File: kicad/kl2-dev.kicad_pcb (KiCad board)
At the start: 2 copper layers, 35.6 x 15.2 mm, 13 parts, among them P1 CONN_13, P2 CONN_13, U1 MKL26Z32VFM4, X1 CRYSTAL

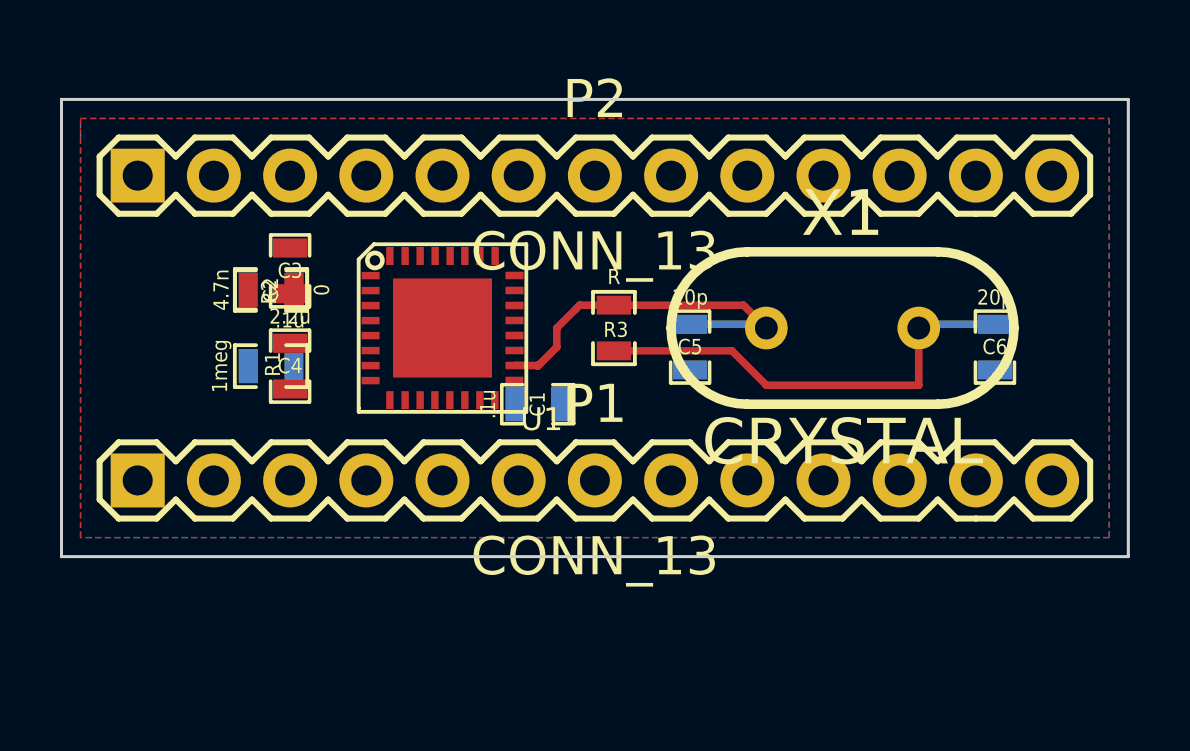
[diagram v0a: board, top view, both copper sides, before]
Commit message: Created initial board with demonstration thermal pad
We need pin 33 to be on its own special net because it shouldn't be
connected. We also have not yet routed the flows.
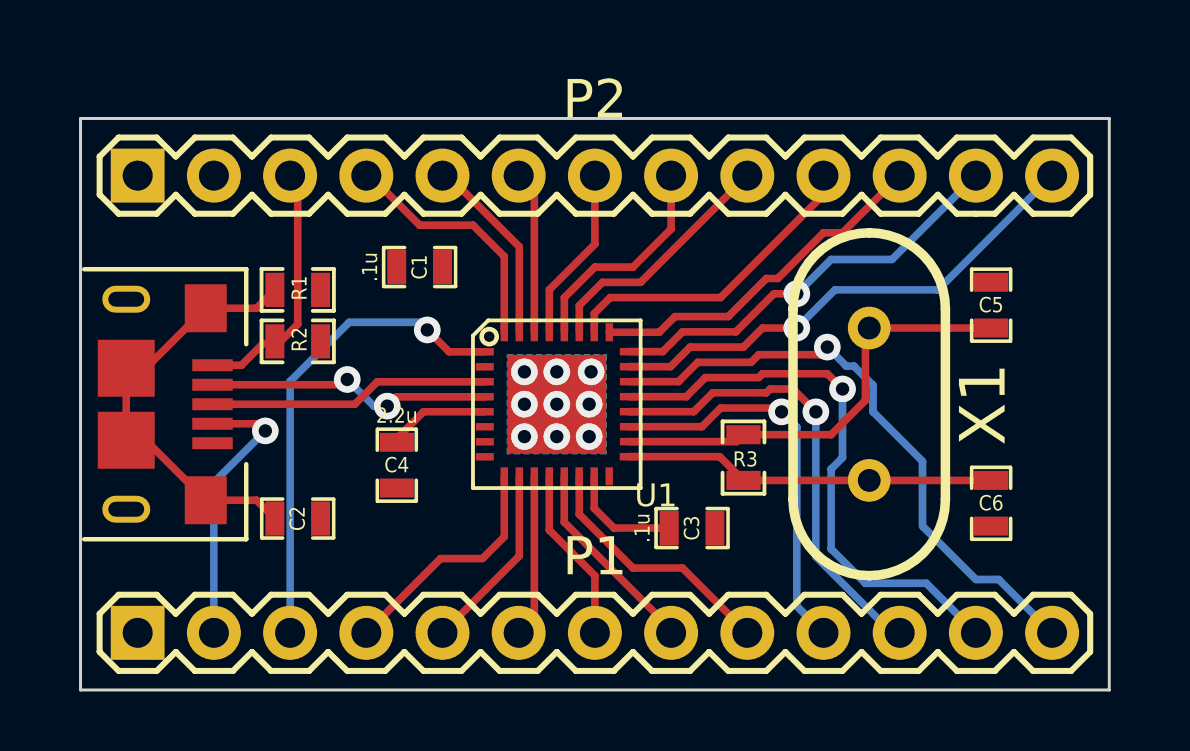
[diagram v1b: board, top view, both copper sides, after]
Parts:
- added CON1: USB-MINI-B, USB-MICRO-B, F.Cu at (36.4, 58.4)
- moved C3 15.9 mm to (55.3, 62.5), turned to 0 degrees
- moved C5 10.1 mm to (65.3, 55.1), turned to 90 degrees
- moved C2 7.67 mm to (42.2, 62.2)
- moved R3 6.11 mm to (57.0, 60.2)
- moved C1 6.03 mm to (46.2, 53.8)
- moved C6 5.21 mm to (65.3, 61.7)
- moved P1 5.08 mm to (52.1, 66.0)
- moved C4 4.85 mm to (45.5, 60.5)
- moved U1 4.58 mm to (50.8, 58.4)
- moved R1 2.69 mm to (42.2, 54.6)
- moved X1 2.69 mm to (61.2, 58.4), turned to 270 degrees
- moved R2 1.93 mm to (42.2, 56.3), turned to 0 degrees
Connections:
- U1 pad 33: (no net) -> GND
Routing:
- net /PTC1: track 0.00 -> 20.3 mm, vias 0 -> 1
- net /PTB1: track 0.00 -> 19.1 mm, vias 0 -> 1
- net /PTC2: track 0.00 -> 16.7 mm, vias 0 -> 1
- net /PTE0: track 0.00 -> 16.1 mm, vias 0 -> 1
- net /PTB0: track 0.00 -> 15.5 mm, vias 0 -> 1
- net N-0000013: track 0.00 -> 14.5 mm
- net /PTC3: track 0.00 -> 14.0 mm, vias 0 -> 1
- net /PTA20: track 0.00 -> 13.3 mm, vias 0 -> 1
- net /PTC4: track 0.00 -> 11.8 mm
- net /PTC5: track 0.00 -> 10.5 mm
- net N-0000012: track 0.00 -> 9.65 mm, vias 0 -> 2
- net N-0000011: track 0.00 -> 9.39 mm
- net /ID: track 0.00 -> 9.30 mm, vias 0 -> 1
- net /PTA4: track 0.00 -> 8.51 mm
- net /PTC6: track 0.00 -> 8.28 mm
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- removed copper zone on F.Cu, net GND
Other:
- board size 35.6 x 15.2 mm -> 34.3 x 19 mm
- net class Default: clearance 0.254 -> 0.1524
- rule trace_clearance: 0.254 -> 0.1524
- rule trace_min: 0.254 -> 0.1524

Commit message: Finished routing all but gnd and thermal pad
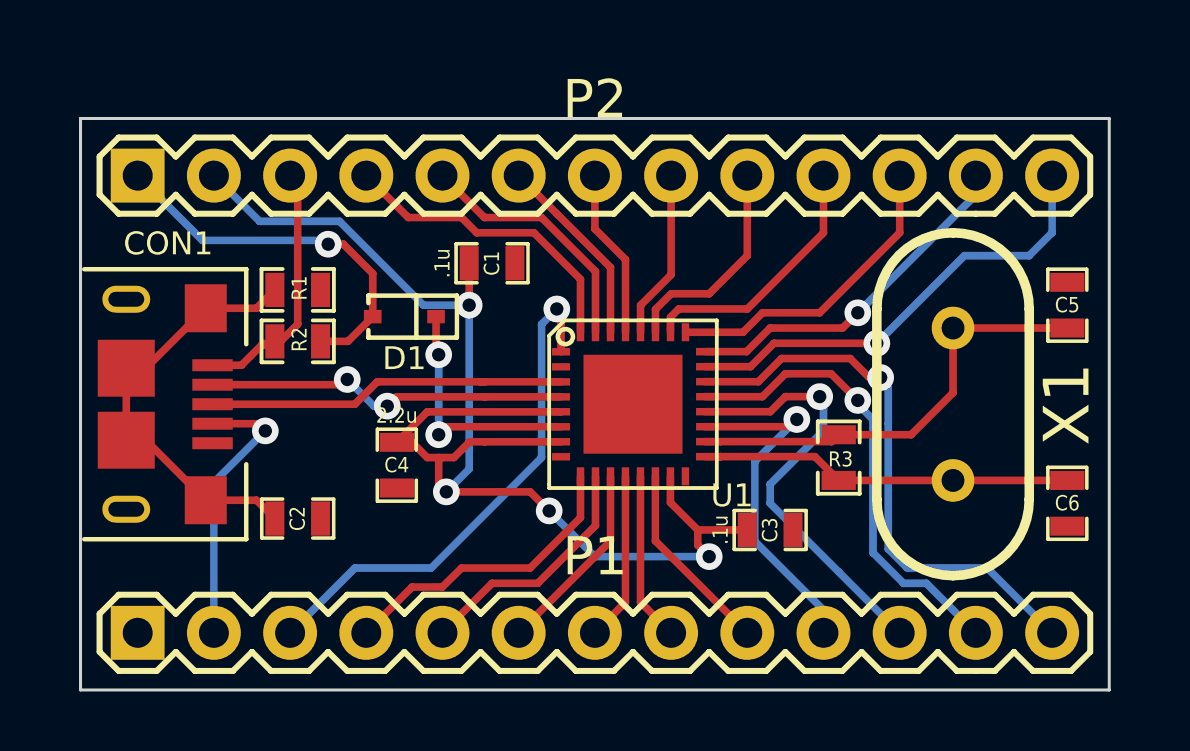
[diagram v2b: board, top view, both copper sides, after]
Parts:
- added D1: DIODE, SOD323, F.Cu at (45.7, 55.5)
- moved R3 3.17 mm to (60.2, 60.2)
- moved X1 2.79 mm to (64.0, 58.4)
- moved C3 2.60 mm to (57.9, 62.6)
- moved U1 2.54 mm to (53.3, 58.4)
- moved C5 2.54 mm to (67.8, 55.1)
- moved C6 2.54 mm to (67.8, 61.7)
- moved C1 2.42 mm to (48.6, 53.7)
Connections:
- U1 pad 33: GND -> /U1_THERM
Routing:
- net +3.3V: track 7.27 -> 45.8 mm, vias 0 -> 4
- net VDD: track 0.00 -> 12.7 mm, vias 0 -> 1
- net N-0000014: track 0.00 -> 8.16 mm, vias 0 -> 2
- net /PTB1: track 19.1 -> 15.6 mm
- net N-0000011: track 9.39 -> 12.1 mm
- net N-0000012: track 9.65 -> 12.2 mm
- net /PTC3: track 14.0 -> 11.8 mm
- net /PTE30: track 7.94 -> 10.1 mm
- net /PTD7: track 8.24 -> 10.3 mm
- net /PTD6: track 6.39 -> 8.45 mm
- net /PTA4: track 8.51 -> 6.49 mm
- net /PTA0: track 6.28 -> 8.22 mm
- net /PTC5: track 10.5 -> 8.67 mm
- net /PTC7: track 7.44 -> 5.64 mm
- net /PTA20: track 13.3 -> 11.8 mm
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- removed copper zone on B.Cu, net GND

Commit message: Added thermal pad and vias
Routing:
- net /U1_THERM: vias 0 -> 9
- added copper zone on B.Cu, net /U1_THERM
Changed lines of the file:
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@@
     (thickness 1.6)
     (drawings 7)
-    (tracks 218)
+    (tracks 227)
     (zones 0)
     (modules 15)
@@
   (segment (start 49.911 63.881) (end 47.625 63.881) (width 0.254) (layer F.Cu) (net 23))
   (segment (start 51.58994 62.20206) (end 49.911 63.881) (width 0.254) (layer F.Cu) (net 23))
+  (via (at 53.34 58.42) (size 0.889) (layers F.Cu B.Cu) (net 24))
+  (via (at 52.324 59.436) (size 0.889) (layers F.Cu B.Cu) (net 24))
+  (via (at 54.356 59.436) (size 0.889) (layers F.Cu B.Cu) (net 24))
+  (via (at 52.324 57.404) (size 0.889) (layers F.Cu B.Cu) (net 24))
+  (via (at 54.356 57.404) (size 0.889) (layers F.Cu B.Cu) (net 24))
+  (via (at 54.356 58.42) (size 0.889) (layers F.Cu B.Cu) (net 24))
+  (via (at 52.324 58.42) (size 0.889) (layers F.Cu B.Cu) (net 24))
+  (via (at 53.34 57.404) (size 0.889) (layers F.Cu B.Cu) (net 24))
+  (via (at 53.34 59.436) (size 0.889) (layers F.Cu B.Cu) (net 24))
   (segment (start 48.26 57.67324) (end 50.94224 57.67324) (width 0.254) (layer F.Cu) (net 26))
   (segment (start 48.40224 57.67324) (end 48.387 57.67324) (width 0.254) (layer F.Cu) (net 26))
@@
   (segment (start 42.926 56.3245) (end 43.8395 56.3245) (width 0.254) (layer F.Cu) (net 33))
   (segment (start 43.8395 56.3245) (end 44.665 55.499) (width 0.254) (layer F.Cu) (net 33))
+  (zone (net 24) (net_name /U1_THERM) (layer B.Cu) (hatch edge 0.508)
+    (connect_pads (clearance 0.508))
+    (min_thickness 0.254)
+    (fill (arc_segments 16) (thermal_gap 5.08) (thermal_bridge_width 5.08))
+    (polygon
+      (pts
+        (xy 51.689 56.769) (xy 54.991 56.769) (xy 54.991 60.071) (xy 51.689 60.071)
+      )
+    )
+  )
 )

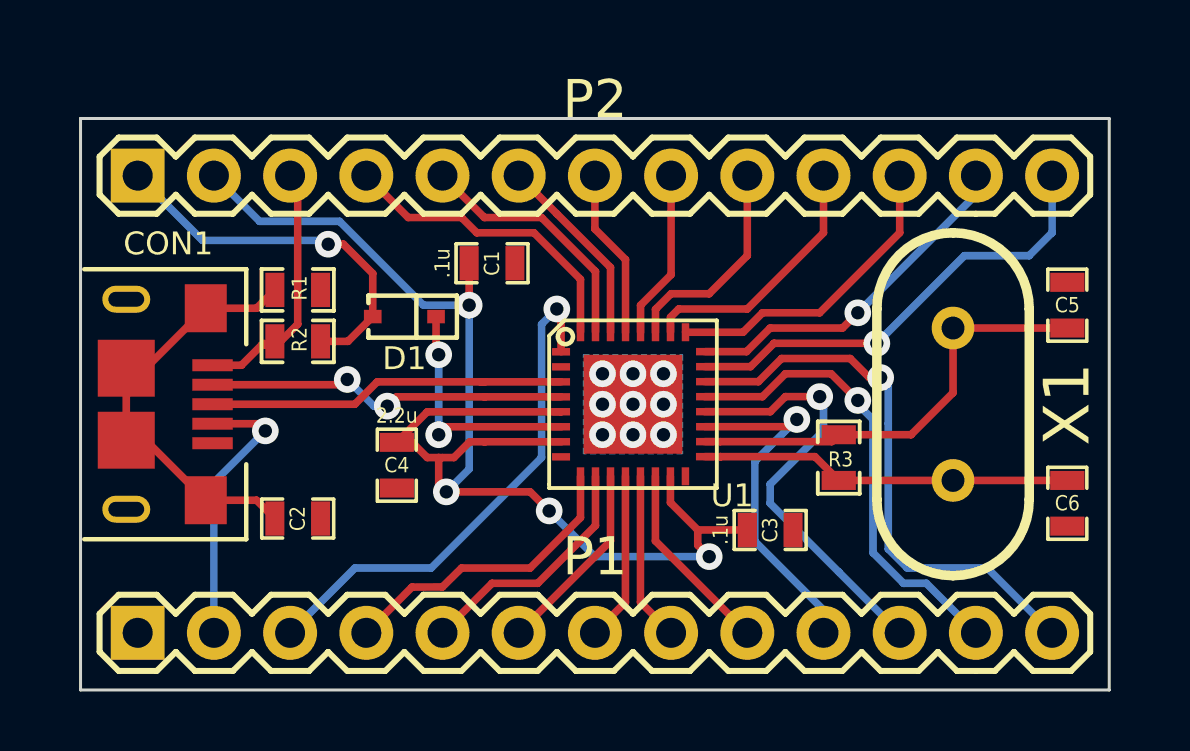
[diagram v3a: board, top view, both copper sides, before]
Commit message: Fixed thermal pad to behave nicely with vias and finished fill
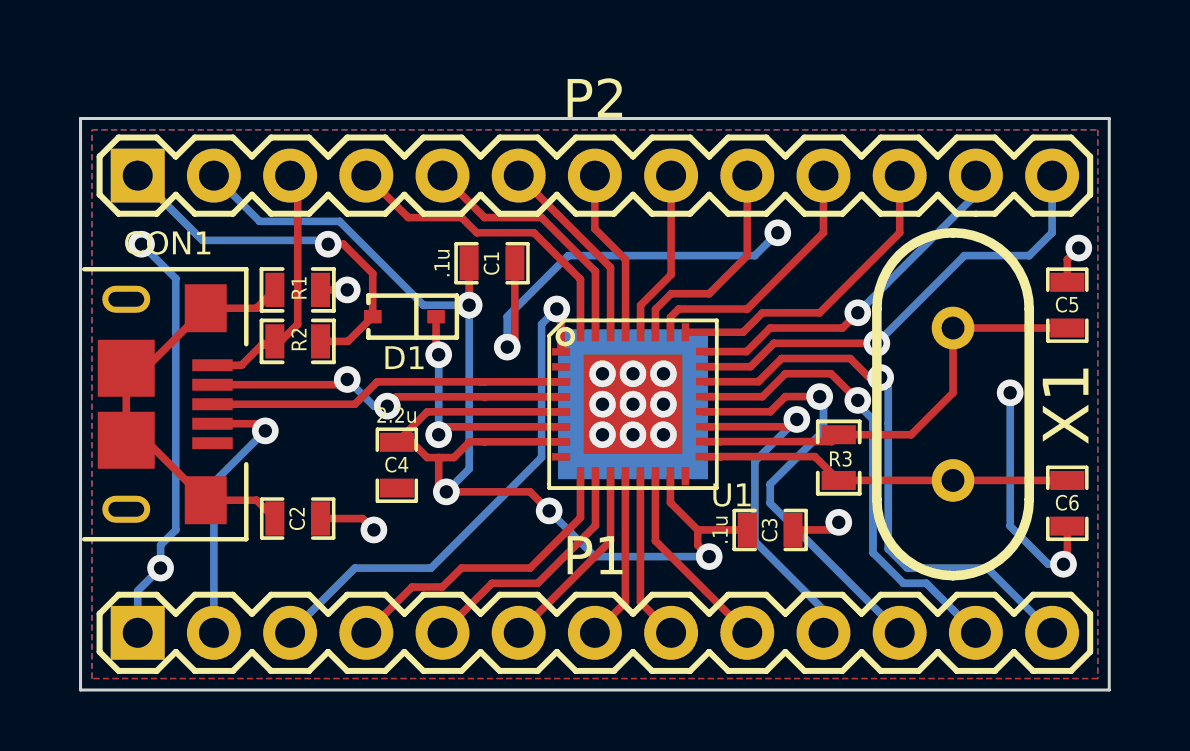
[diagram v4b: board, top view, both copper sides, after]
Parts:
- added P3: TST, THERM5x5, B.Cu at (53.3, 58.4)
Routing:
- net GND: track 0.00 -> 41.9 mm, vias 0 -> 10
- added copper zone on B.Cu, net GND
- added copper zone on F.Cu, net GND
- removed copper zone on B.Cu, net /U1_THERM
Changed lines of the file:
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@@
 (kicad_pcb (version 3) (host pcbnew "(2013-may-18)-stable")
   (general
-    (links 57)
-    (no_connects 11)
+    (links 58)
+    (no_connects 1)
     (area 34.874999 48.844999 69.265001 67.995001)
     (thickness 1.6)
     (drawings 7)
-    (tracks 227)
+    (tracks 261)
     (zones 0)
-    (modules 15)
+    (modules 16)
     (nets 34)
   )
@@
     (last_trace_width 0.254)
     (trace_clearance 0.1524)
-    (zone_clearance 0.508)
+    (zone_clearance 0.254)
     (zone_45_only no)
     (trace_min 0.1524)
@@
     (mod_text_size 1 1)
     (mod_text_width 0.15)
-    (pad_size 3.29946 3.29946)
+    (pad_size 5 5)
     (pad_drill 0)
     (pad_to_mask_clearance 0)
@@
       (layers F.Cu F.Paste F.Mask)
       (net 29 N-0000014)
+    )
+  )
+  (module THERM5x5 (layer B.Cu)
+    (at 53.34 58.42)
+    (fp_text reference P3 (at 0 -3.6) (layer B.SilkS) hide
+      (effects (font (size 1 1) (thickness 0.15)) (justify mirror))
+    )
+    (fp_text value TST (at 0 3.5) (layer B.SilkS) hide
+      (effects (font (size 0.7 0.7) (thickness 0.07)) (justify mirror))
+    )
+    (pad 1 smd rect (at 0 0) (size 5 5)
+      (layers B.Cu B.Paste B.Mask)
+      (net 24 /U1_THERM)
     )
   )
@@
   (via (at 52.324 57.404) (size 0.889) (layers F.Cu B.Cu) (net 24))
   (via (at 54.356 57.404) (size 0.889) (layers F.Cu B.Cu) (net 24))
+  (via (at 52.324 58.42) (size 0.889) (layers F.Cu B.Cu) (net 24))
+  (via (at 53.34 59.436) (size 0.889) (layers F.Cu B.Cu) (net 24))
   (via (at 54.356 58.42) (size 0.889) (layers F.Cu B.Cu) (net 24))
-  (via (at 52.324 58.42) (size 0.889) (layers F.Cu B.Cu) (net 24))
   (via (at 53.34 57.404) (size 0.889) (layers F.Cu B.Cu) (net 24))
-  (via (at 53.34 59.436) (size 0.889) (layers F.Cu B.Cu) (net 24))
+  (segment (start 49.149 56.515) (end 49.149 55.499) (width 0.254) (layer B.Cu) (net 25))
+  (segment (start 49.403 56.261) (end 49.149 56.515) (width 0.254) (layer F.Cu) (net 25))
+  (via (at 49.149 56.515) (size 0.889) (layers F.Cu B.Cu) (net 25))
+  (segment (start 49.403 53.721) (end 49.403 56.261) (width 0.254) (layer F.Cu) (net 25))
+  (via (at 58.166 52.705) (size 0.889) (layers F.Cu B.Cu) (net 25))
+  (segment (start 57.404 53.467) (end 58.166 52.705) (width 0.254) (layer B.Cu) (net 25))
+  (segment (start 51.181 53.467) (end 57.404 53.467) (width 0.254) (layer B.Cu) (net 25))
+  (segment (start 49.149 55.499) (end 51.181 53.467) (width 0.254) (layer B.Cu) (net 25))
+  (segment (start 37.592 63.881) (end 37.592 63.119) (width 0.254) (layer B.Cu) (net 25))
+  (segment (start 36.83 64.643) (end 37.592 63.881) (width 0.254) (layer B.Cu) (net 25))
+  (via (at 37.592 63.881) (size 0.889) (layers F.Cu B.Cu) (net 25))
+  (segment (start 36.83 66.04) (end 36.83 64.643) (width 0.254) (layer B.Cu) (net 25))
+  (via (at 36.957 53.086) (size 0.889) (layers F.Cu B.Cu) (net 25))
+  (segment (start 38.1 54.229) (end 36.957 53.086) (width 0.254) (layer B.Cu) (net 25))
+  (segment (start 38.1 62.611) (end 38.1 54.229) (width 0.254) (layer B.Cu) (net 25))
+  (segment (start 37.592 63.119) (end 38.1 62.611) (width 0.254) (layer B.Cu) (net 25))
+  (segment (start 42.926 62.23) (end 44.323 62.23) (width 0.254) (layer F.Cu) (net 25))
+  (via (at 44.704 62.611) (size 0.889) (layers F.Cu B.Cu) (net 25))
+  (segment (start 44.323 62.23) (end 44.704 62.611) (width 0.254) (layer F.Cu) (net 25))
+  (segment (start 67.691 63.754) (end 67.183 63.754) (width 0.254) (layer B.Cu) (net 25))
+  (segment (start 67.818 63.627) (end 67.691 63.754) (width 0.254) (layer F.Cu) (net 25))
+  (via (at 67.691 63.754) (size 0.889) (layers F.Cu B.Cu) (net 25))
+  (segment (start 67.818 62.484) (end 67.818 63.627) (width 0.254) (layer F.Cu) (net 25))
+  (via (at 65.913 58.039) (size 0.889) (layers F.Cu B.Cu) (net 25))
+  (segment (start 65.913 62.484) (end 65.913 58.039) (width 0.254) (layer B.Cu) (net 25))
+  (segment (start 67.183 63.754) (end 65.913 62.484) (width 0.254) (layer B.Cu) (net 25))
+  (segment (start 67.818 54.356) (end 67.818 53.594) (width 0.254) (layer F.Cu) (net 25))
+  (via (at 68.199 53.213) (size 0.889) (layers F.Cu B.Cu) (net 25))
+  (segment (start 67.818 53.594) (end 68.199 53.213) (width 0.254) (layer F.Cu) (net 25))
+  (segment (start 58.674 62.611) (end 59.944 62.611) (width 0.254) (layer F.Cu) (net 25))
+  (via (at 60.198 62.357) (size 0.889) (layers F.Cu B.Cu) (net 25))
+  (segment (start 59.944 62.611) (end 60.198 62.357) (width 0.254) (layer F.Cu) (net 25))
+  (segment (start 42.926 54.61) (end 43.815 54.61) (width 0.254) (layer F.Cu) (net 25))
+  (via (at 43.815 54.61) (size 0.889) (layers F.Cu B.Cu) (net 25))
   (segment (start 48.26 57.67324) (end 50.94224 57.67324) (width 0.254) (layer F.Cu) (net 26))
   (segment (start 48.40224 57.67324) (end 48.387 57.67324) (width 0.254) (layer F.Cu) (net 26))
@@
   (segment (start 42.926 56.3245) (end 43.8395 56.3245) (width 0.254) (layer F.Cu) (net 33))
   (segment (start 43.8395 56.3245) (end 44.665 55.499) (width 0.254) (layer F.Cu) (net 33))
-  (zone (net 24) (net_name /U1_THERM) (layer B.Cu) (hatch edge 0.508)
-    (connect_pads (clearance 0.508))
-    (min_thickness 0.254)
-    (fill (arc_segments 16) (thermal_gap 5.08) (thermal_bridge_width 5.08))
+  (zone (net 25) (net_name GND) (layer F.Cu) (hatch edge 0.508)
+    (connect_pads (clearance 0.254))
+    (min_thickness 0.1524)
+    (fill (arc_segments 16) (thermal_gap 0.1524) (thermal_bridge_width 0.254) (smoothing fillet) (radius 0.508))
     (polygon
       (pts
-        (xy 51.689 56.769) (xy 54.991 56.769) (xy 54.991 60.071) (xy 51.689 60.071)
+        (xy 35.306 49.276) (xy 68.834 49.276) (xy 68.834 67.564) (xy 35.306 67.564)
       )
     )
+  )
+  (zone (net 25) (net_name GND) (layer B.Cu) (hatch edge 0.508)
+    (connect_pads (clearance 0.254))
+    (min_thickness 0.1524)
+    (fill (arc_segments 16) (thermal_gap 0.1524) (thermal_bridge_width 0.254) (smoothing fillet) (radius 0.508))
+    (polygon
+      (pts
+        (xy 35.306 49.276) (xy 68.834 49.276) (xy 68.834 67.564) (xy 35.306 67.564)
+      )
+    )
